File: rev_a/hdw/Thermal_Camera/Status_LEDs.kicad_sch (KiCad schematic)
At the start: 20 parts, among them U1601 74LVC1G97, U1602 74LVC1G97, U1603 74LVC1G97, U1604 74LVC1G97

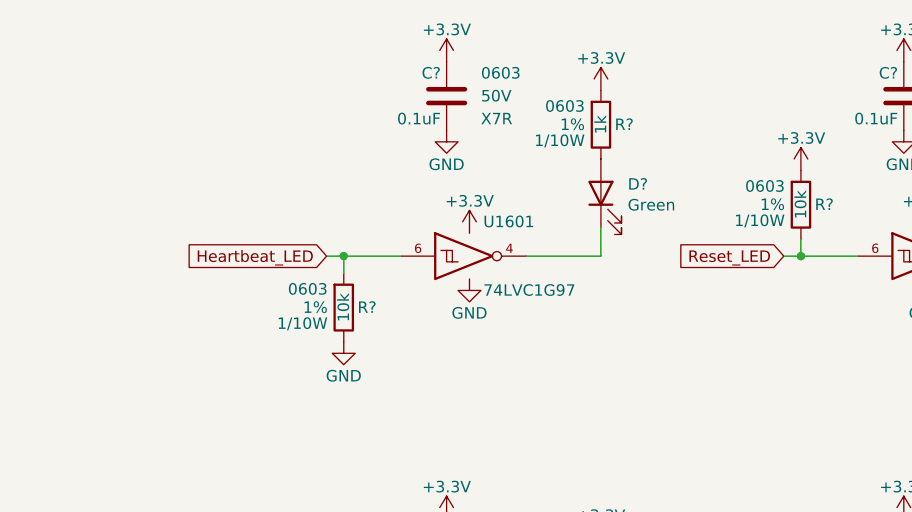
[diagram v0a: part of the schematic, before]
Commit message: added lepton sensor, made some other schematic progress
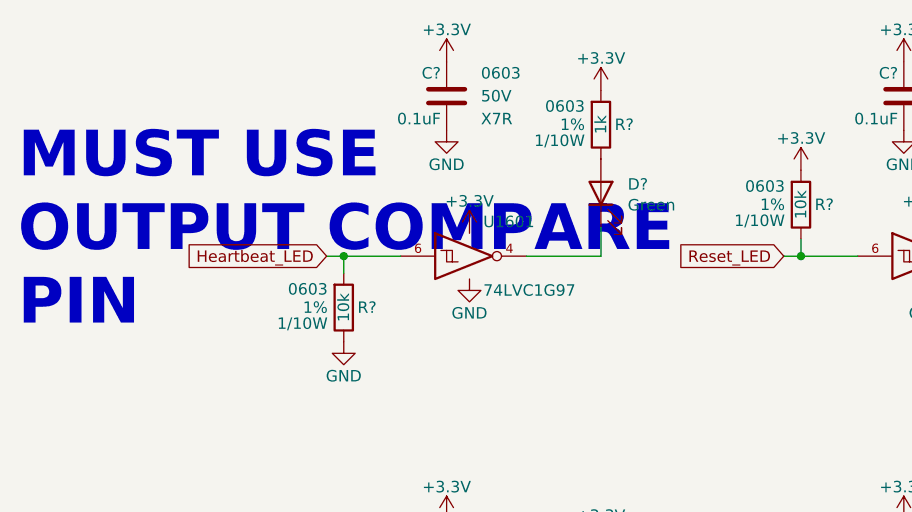
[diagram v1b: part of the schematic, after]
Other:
- note added: "MUST USE OUTPUT COMPARE PIN"
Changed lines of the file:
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@@
   (title_block
     (title "Thermal Camera")
-    (date "2023-11-11")
+    (date "2023-11-12")
     (rev "PRELIM")
     (company "Drew Maatman and Michael Laffin")
@@
     (stroke (width 0) (type default))
   )
+  (text "MUST USE\nOUTPUT COMPARE\nPIN" (at 55.88 83.185 0)
+    (effects (font (size 5.08 5.08) (thickness 1.016) bold (color 194 0 0 1)) (justify left bottom))
+  )
   (global_label "Heartbeat_LED" (shape input) (at 90.17 74.93 180) (fields_autoplaced)

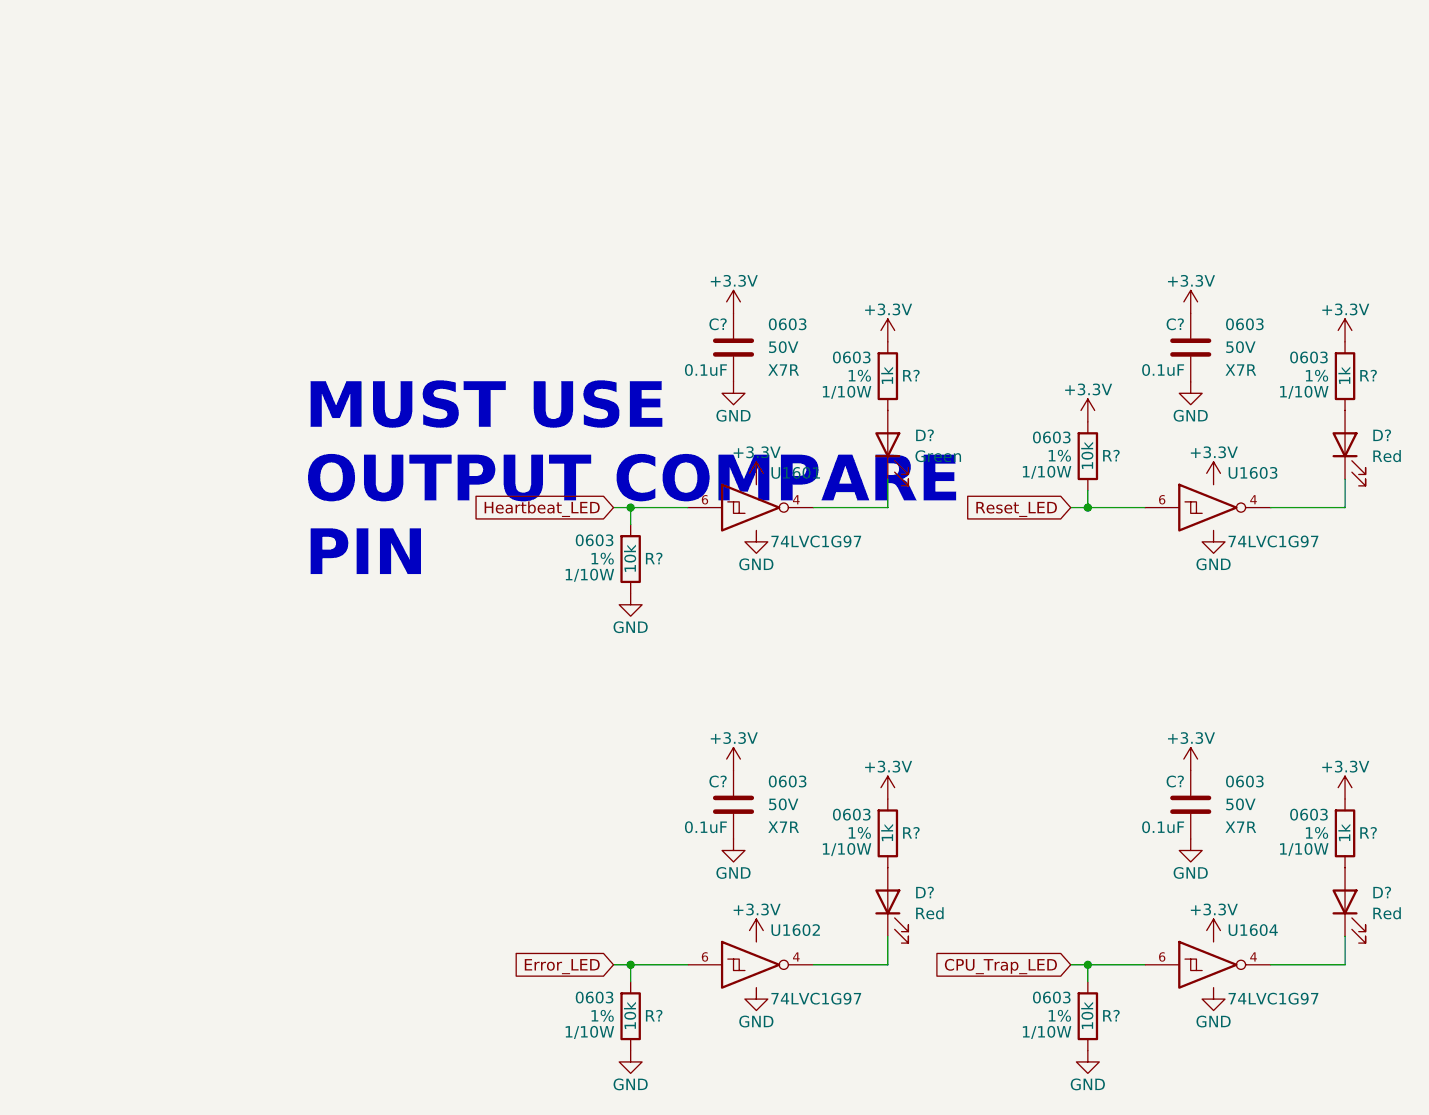
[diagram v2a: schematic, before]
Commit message: changed a lot of circuits from +3.3V to +3.0V VDD
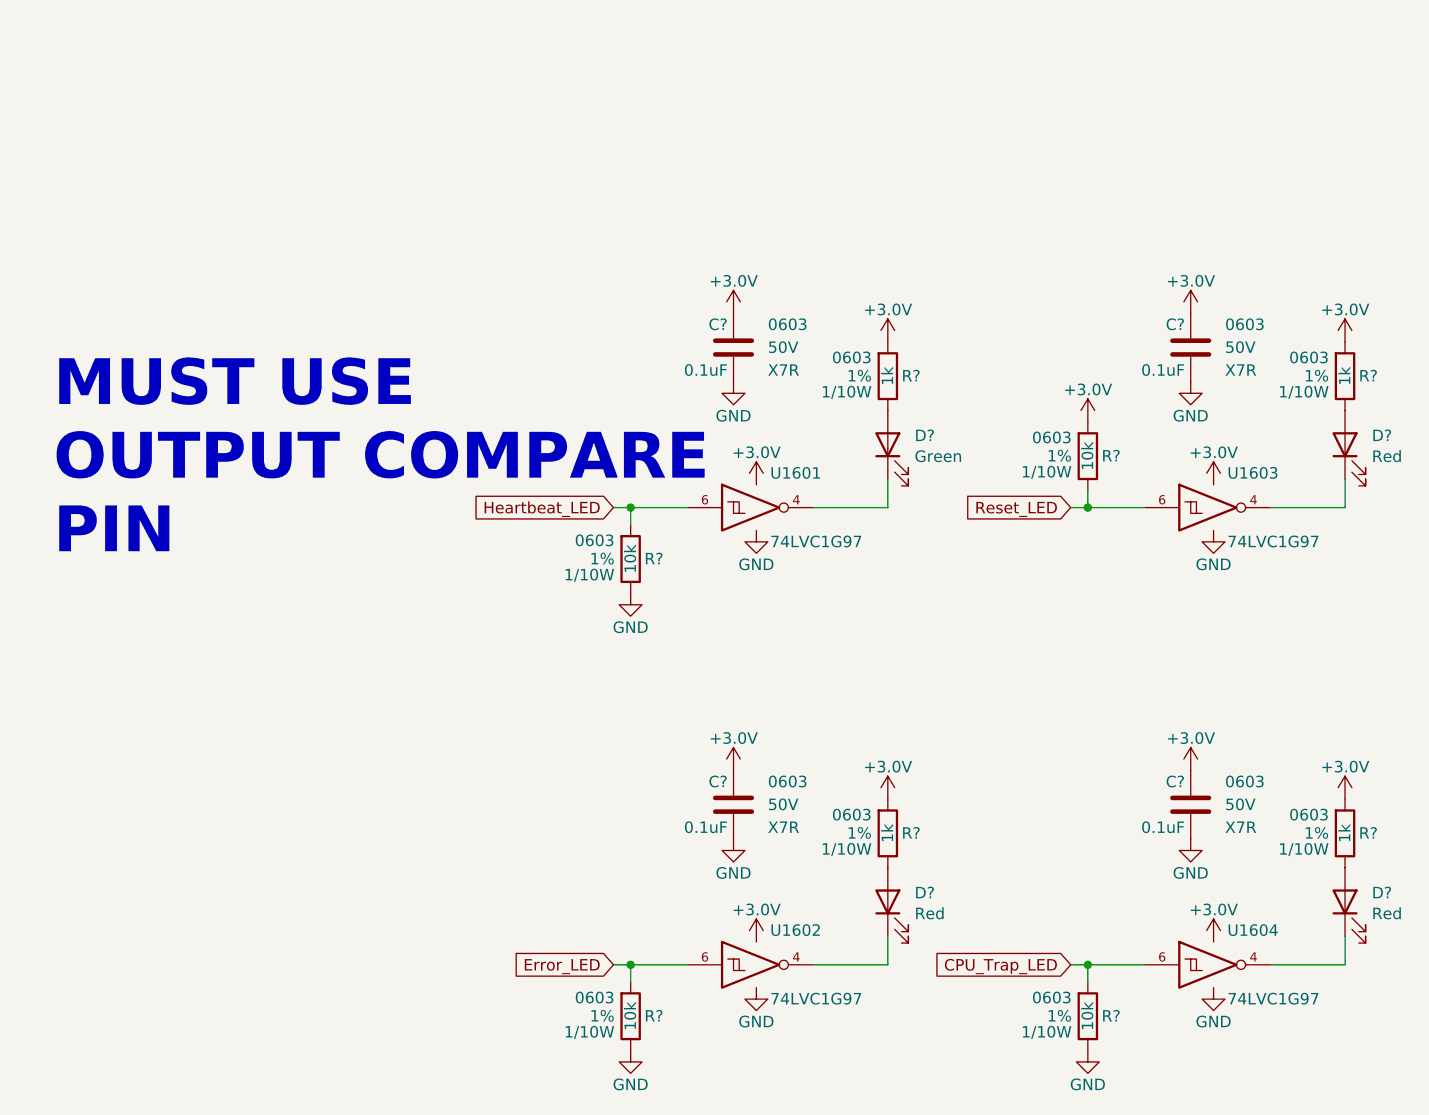
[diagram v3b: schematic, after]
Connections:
- net +3.3V renamed +3.0V

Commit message: blah blah
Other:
- note removed: "MUST USE OUTPUT COMPARE PIN"
- moved on the sheet: C?, D?, R?, U1601, U1602, U1603, U1604

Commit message: lots of schematic progress
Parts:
- C? (x4): footprint Capacitors_SMD:C_0603 -> (none); Digi-Key PN 1276-1935-1-ND -> (none); display_footprint 0603 -> (none)
- D?: footprint LEDs:LED_0603 -> (none); Digi-Key PN 754-1121-1-ND -> (none)
- D? (x3): footprint LEDs:LED_0603 -> (none); Digi-Key PN 754-1117-1-ND -> (none)
- R? (x4): footprint Resistors_SMD:R_0603 -> (none); Digi-Key PN 541-10.0KHCT-ND -> (none); Wattage 1/10W -> (none); display_footprint 0603 -> (none)
- R? (x4): footprint Resistors_SMD:R_0603 -> (none); Digi-Key PN 541-1.00KHCT-ND -> (none); Wattage 1/10W -> (none); display_footprint 0603 -> (none)
- renumbered U1604 to U?, U1603 to U?, U1601 to U?, U1602 to U?

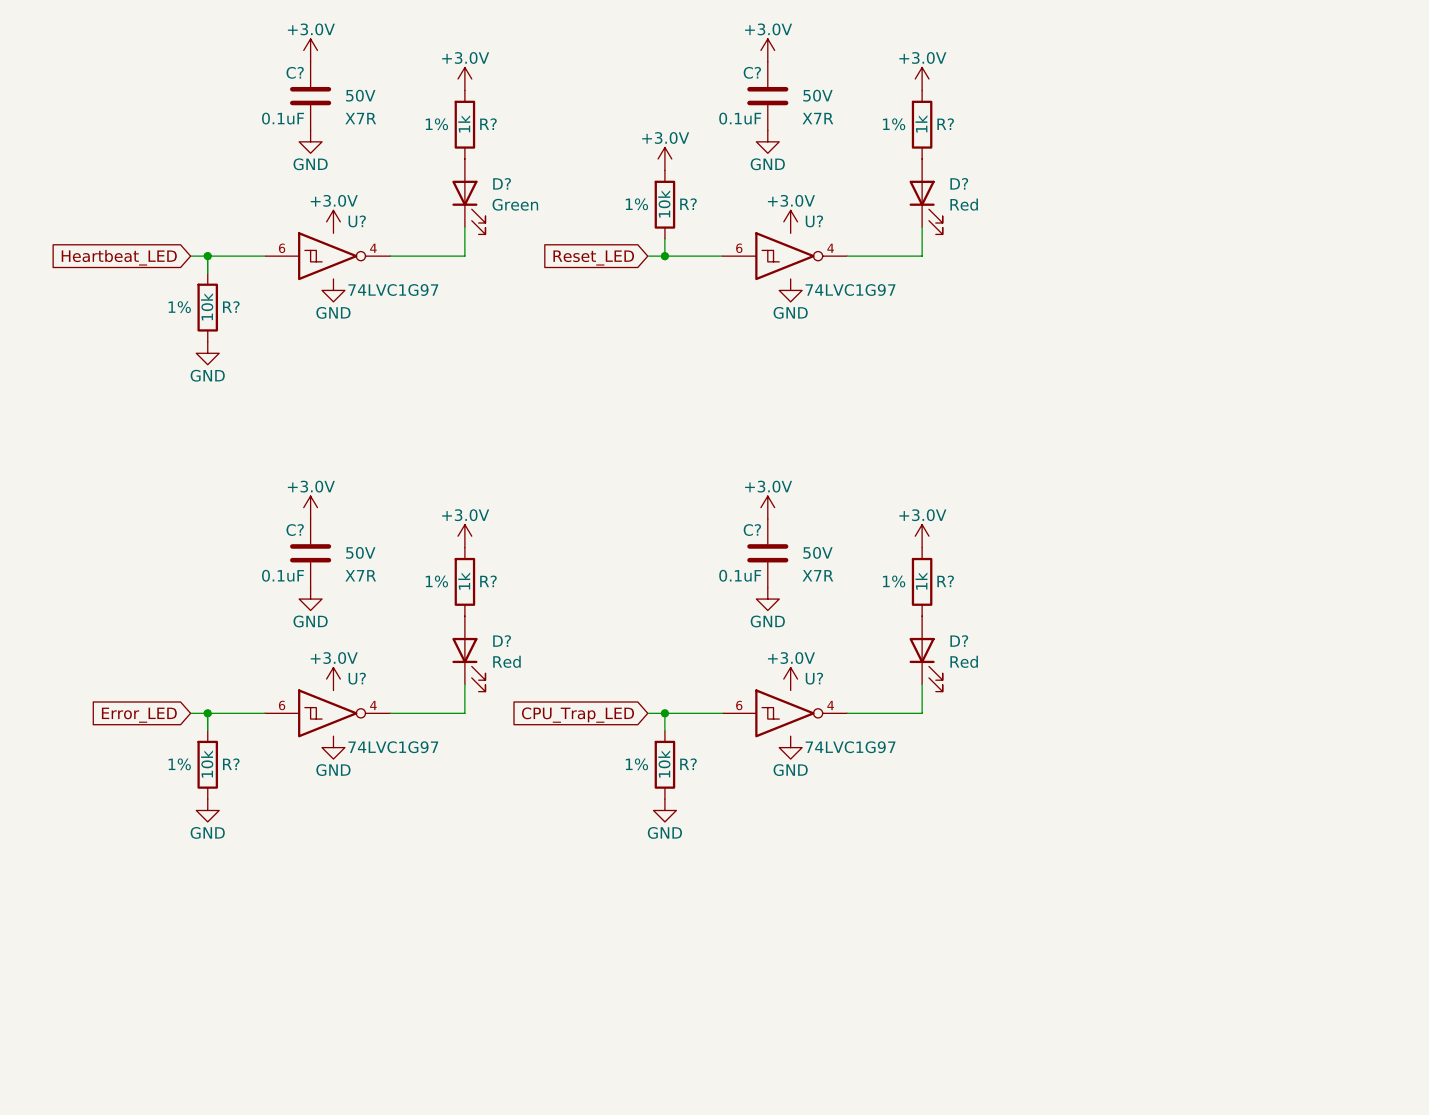
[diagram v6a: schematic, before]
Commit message: assigned a ton of footprints
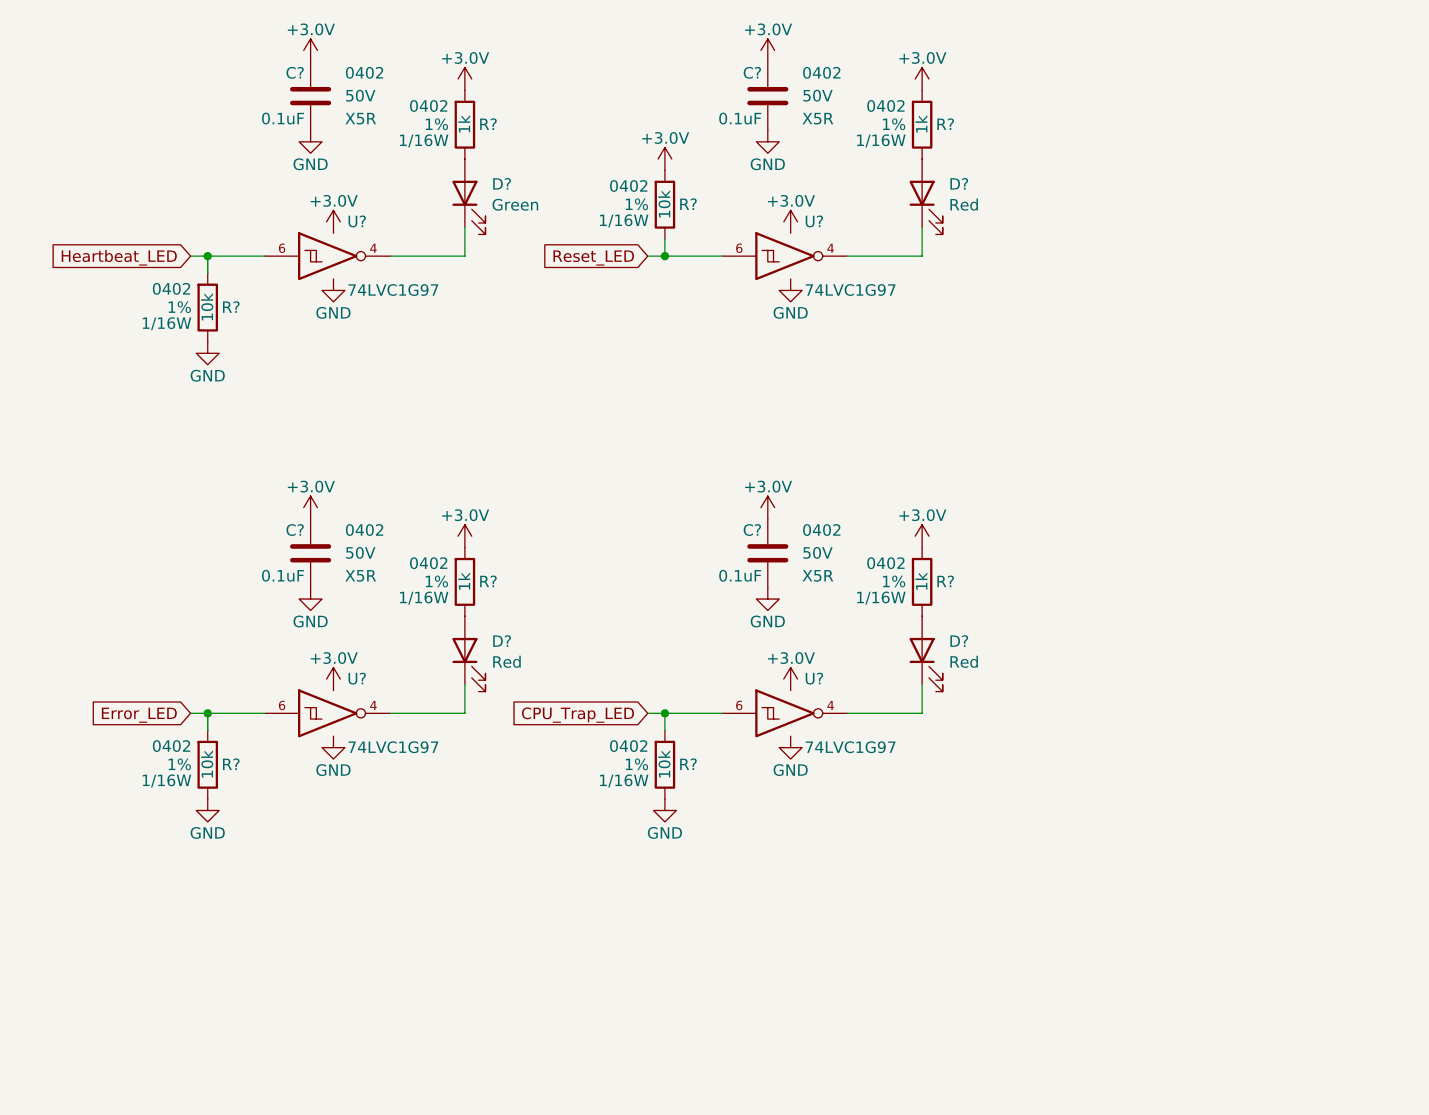
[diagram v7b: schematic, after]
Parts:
- C? (x4): footprint (none) -> Capacitors_SMD:C_0402; Dielectric X7R -> X5R; display_footprint (none) -> 0402
- D? (x4): footprint (none) -> LEDs:LED_0402
- R? (x8): footprint (none) -> Resistors_SMD:R_0402; Wattage (none) -> 1/16W; display_footprint (none) -> 0402
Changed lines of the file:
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@@
 			)
 		)
-		(property "Footprint" ""
+		(property "Footprint" "Capacitors_SMD:C_0402"
 			(at 106.3498 83.82 0)
 			(effects
@@
 			)
 		)
-		(property "display_footprint" ""
+		(property "display_footprint" "0402"
 			(at 111.125 77.47 0)
 			(effects
@@
 			)
 		)
-		(property "Dielectric" "X7R"
+		(property "Dielectric" "X5R"
 			(at 111.125 82.55 0)
 			(effects
@@
 			)
 		)
-		(property "Footprint" ""
+		(property "Footprint" "LEDs:LED_0402"
 			(at 73.66 40.005 0)
 			(effects
@@
 			)
 		)
-		(property "Footprint" ""
+		(property "Footprint" "Capacitors_SMD:C_0402"
 			(at 55.5498 83.82 0)
 			(effects
@@
 			)
 		)
-		(property "display_footprint" ""
+		(property "display_footprint" "0402"
 			(at 60.325 77.47 0)
 			(effects
@@
 			)
 		)
-		(property "Dielectric" "X7R"
+		(property "Dielectric" "X5R"
 			(at 60.325 82.55 0)
 			(effects
@@
 			)
 		)
-		(property "Footprint" ""
+		(property "Footprint" "Capacitors_SMD:C_0402"
 			(at 55.5498 33.02 0)
 			(effects
@@
 			)
 		)
-		(property "display_footprint" ""
+		(property "display_footprint" "0402"
 			(at 60.325 26.67 0)
 			(effects
@@
 			)
 		)
-		(property "Dielectric" "X7R"
+		(property "Dielectric" "X5R"
 			(at 60.325 31.75 0)
 			(effects
@@
 			)
 		)
-		(property "Footprint" ""
+		(property "Footprint" "Resistors_SMD:R_0402"
 			(at 95.885 103.505 0)
 			(effects
@@
 			)
 		)
-		(property "display_footprint" ""
+		(property "display_footprint" "0402"
 			(at 94.107 101.473 0)
 			(effects
@@
 			)
 		)
-		(property "Wattage" ""
+		(property "Wattage" "1/16W"
 			(at 94.107 105.283 0)
 			(effects
@@
 			)
 		)
-		(property "Footprint" ""
+		(property "Footprint" "Resistors_SMD:R_0402"
 			(at 73.66 32.385 0)
 			(effects
@@
 			)
 		)
-		(property "display_footprint" ""
+		(property "display_footprint" "0402"
 			(at 71.882 30.353 0)
 			(effects
@@
 			)
 		)
-		(property "Wattage" ""
+		(property "Wattage" "1/16W"
 			(at 71.882 34.163 0)
 			(effects
@@
 			)
 		)
-		(property "Footprint" ""
+		(property "Footprint" "Resistors_SMD:R_0402"
 			(at 95.885 41.275 0)
 			(effects
@@
 			)
 		)
-		(property "display_footprint" ""
+		(property "display_footprint" "0402"
 			(at 94.107 39.243 0)
 			(effects
@@
 			)
 		)
-		(property "Wattage" ""
+		(property "Wattage" "1/16W"
 			(at 94.107 43.053 0)
 			(effects
@@
 			)
 		)
-		(property "Footprint" ""
+		(property "Footprint" "Resistors_SMD:R_0402"
 			(at 124.46 32.385 0)
 			(effects
@@
 			)
 		)
-		(property "display_footprint" ""
+		(property "display_footprint" "0402"
 			(at 122.682 30.353 0)
 			(effects
@@
 			)
 		)
-		(property "Wattage" ""
+		(property "Wattage" "1/16W"
 			(at 122.682 34.163 0)
 			(effects
@@
 			)
 		)
-		(property "Footprint" ""
+		(property "Footprint" "Resistors_SMD:R_0402"
 			(at 45.085 52.705 0)
 			(effects
@@
 			)
 		)
-		(property "display_footprint" ""
+		(property "display_footprint" "0402"
 			(at 43.307 50.673 0)
 			(effects
@@
 			)
 		)
-		(property "Wattage" ""
+		(property "Wattage" "1/16W"
 			(at 43.307 54.483 0)
 			(effects
@@
 			)
 		)
-		(property "Footprint" ""
+		(property "Footprint" "Resistors_SMD:R_0402"
 			(at 45.085 103.505 0)
 			(effects
@@
 			)
 		)
-		(property "display_footprint" ""
+		(property "display_footprint" "0402"
 			(at 43.307 101.473 0)
 			(effects
@@
 			)
 		)
-		(property "Wattage" ""
+		(property "Wattage" "1/16W"
 			(at 43.307 105.283 0)
 			(effects
@@
 			)
 		)
-		(property "Footprint" ""
+		(property "Footprint" "Resistors_SMD:R_0402"
 			(at 73.66 83.185 0)
 			(effects
@@
 			)
 		)
-		(property "display_footprint" ""
+		(property "display_footprint" "0402"
 			(at 71.882 81.153 0)
 			(effects
@@
 			)
 		)
-		(property "Wattage" ""
+		(property "Wattage" "1/16W"
 			(at 71.882 84.963 0)
 			(effects
@@
 			)
 		)
-		(property "Footprint" ""
+		(property "Footprint" "Resistors_SMD:R_0402"
 			(at 124.46 83.185 0)
 			(effects
@@
 			)
 		)
-		(property "display_footprint" ""
+		(property "display_footprint" "0402"
 			(at 122.682 81.153 0)
 			(effects
@@
 			)
 		)
-		(property "Wattage" ""
+		(property "Wattage" "1/16W"
 			(at 122.682 84.963 0)
 			(effects
@@
 			)
 		)
-		(property "Footprint" ""
+		(property "Footprint" "LEDs:LED_0402"
 			(at 73.66 90.805 0)
 			(effects
@@
 			)
 		)
-		(property "Footprint" ""
+		(property "Footprint" "LEDs:LED_0402"
 			(at 124.46 90.805 0)
 			(effects
@@
 			)
 		)
-		(property "Footprint" ""
+		(property "Footprint" "LEDs:LED_0402"
 			(at 124.46 40.005 0)
 			(effects
@@
 			)
 		)
-		(property "Footprint" ""
+		(property "Footprint" "Capacitors_SMD:C_0402"
 			(at 106.3498 33.02 0)
 			(effects
@@
 			)
 		)
-		(property "display_footprint" ""
+		(property "display_footprint" "0402"
 			(at 111.125 26.67 0)
 			(effects
@@
 			)
 		)
-		(property "Dielectric" "X7R"
+		(property "Dielectric" "X5R"
 			(at 111.125 31.75 0)
 			(effects
